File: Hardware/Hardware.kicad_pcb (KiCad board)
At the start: 2 copper layers, 91.4 x 142.2 mm, 47 parts, among them J1 Conn_01x04_Pin, J2 RJ45_LED_Shielded, J3 USB_A, SW1 SW_SPST, SW2 SW_Push, SW3 SW_Push, SW4 SW_Push, SW5 SW_Push, SW6 SW_Push, SW7 SW_Push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

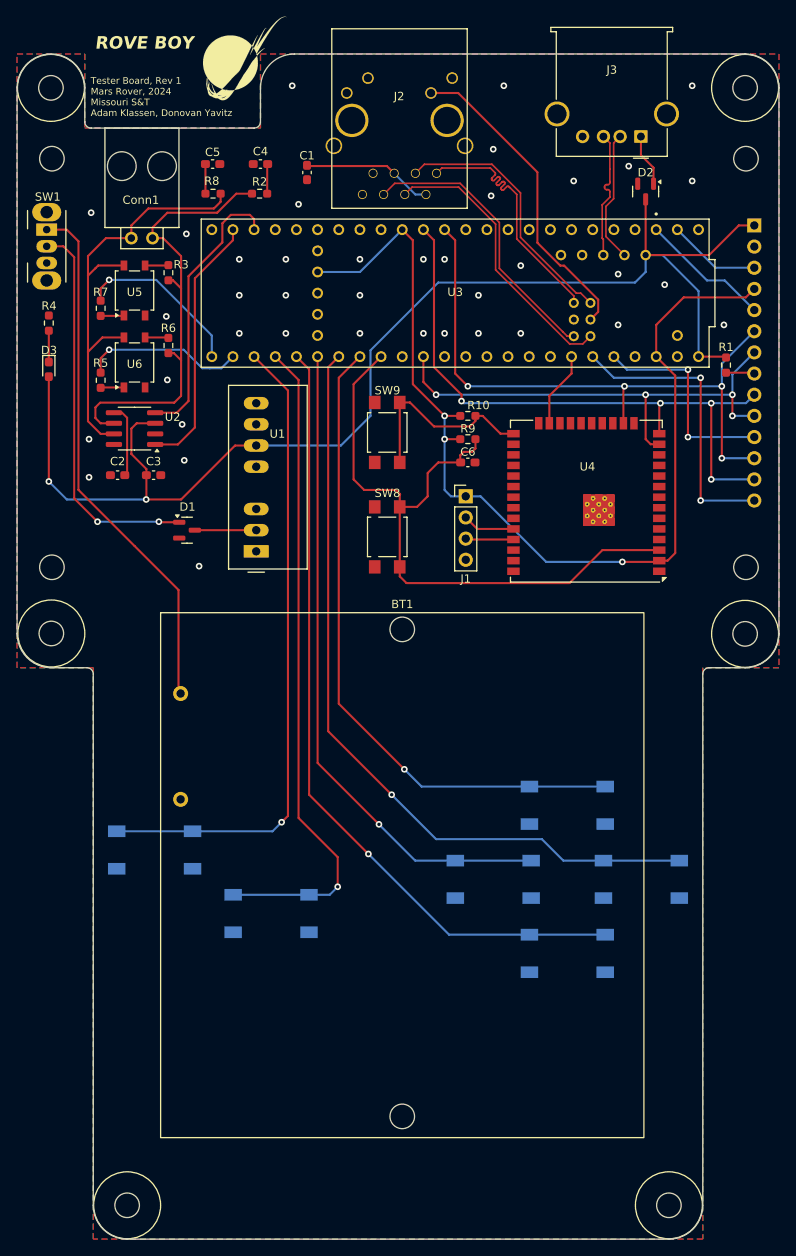
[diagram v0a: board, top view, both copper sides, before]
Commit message: fixed silkscreens and added servo tester
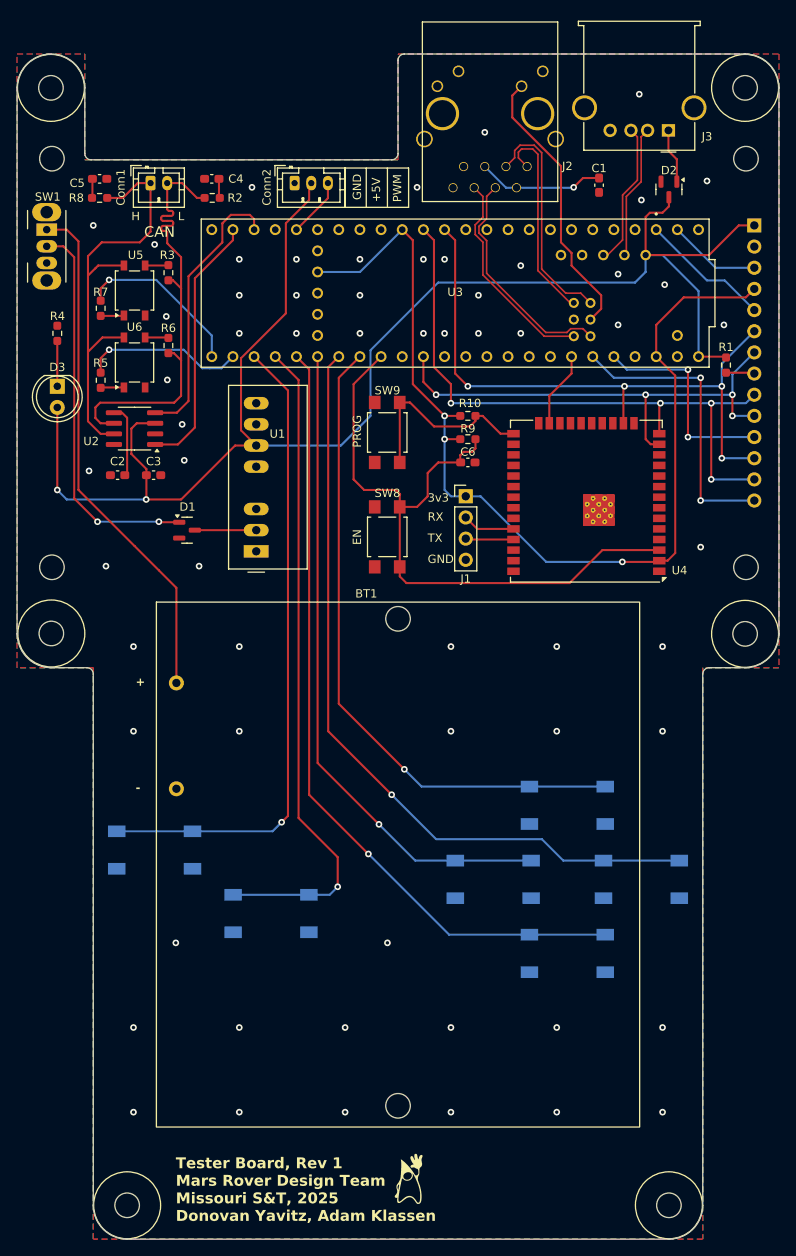
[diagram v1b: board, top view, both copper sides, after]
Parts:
- removed the G*** at (181.0, 61.5)
- added Conn2: Molex_SL_03, Connector_JST:JST_PH_B3B-PH-K_1x03_P2.00mm_Vertical, F.Cu at (187.0, 76.5)
- added G***: LOGO, Tester:duke, F.Cu at (200.7, 196.1)
- Conn1: footprint MRDT_Connectors:MOLEX_SL_02_Horizontal -> Connector_JST:JST_PH_B2B-PH-K_1x02_P2.00mm_Vertical
- D3: footprint LED_SMD:LED_0603_1608Metric_Pad1.05x0.95mm_HandSolder -> LED_THT:LED_D5.0mm
- moved C1 35.1 mm to (223.5, 76.7)
- moved C5 13.7 mm to (163.6, 75.9)
- moved R8 13.6 mm to (163.6, 78.2)
- moved J2 10.9 mm to (210.3, 55.1)
- moved Conn1 6.99 mm to (169.7, 76.5)
- moved C4 6.11 mm to (177.0, 75.9)
- moved R2 5.71 mm to (177.1, 78.2)
- moved J3 3.38 mm to (231.8, 70.1)
- moved D2 2.81 mm to (231.9, 77.2)
- moved D3 2.27 mm to (158.5, 100.8)
- moved R4 1.60 mm to (158.5, 94.5)
- moved BT1 1.37 mm to (199.4, 126.7)
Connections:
- U3 pad 28: unconnected-(U3-RX7-Pad28) -> PWM
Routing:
- net +5V: track 156.3 -> 190.4 mm
- net Rx-: track 34.2 -> 25.6 mm
- net PWM: track 0.00 -> 7.15 mm
- net Rx+: track 34.1 -> 27.4 mm
- net Tx+: track 31.4 -> 24.8 mm
- net LED: track 38.1 -> 33.4 mm
- net Tx-: track 31.5 -> 27.7 mm
- net Net-(D3-K): track 3.76 -> 5.44 mm
- net Net-(BT1-+): track 63.7 -> 62.3 mm
- net USB_D+: track 15.8 -> 17.3 mm
- net Net-(C4-Pad1): track 3.58 -> 2.33 mm
- net Net-(C5-Pad1): track 3.56 -> 2.31 mm
- net MISO: track 76.4 -> 77.3 mm
- net Net-(C1-Pad1): track 15.7 -> 15.3 mm, vias 0 -> 1
- net GND: vias 39 -> 61
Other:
- outline, holes or cut-outs redrawn
- board text added: "+"
- board text added: "+5V"
- board text added: "-"
- board text added: "3v3"
- board text added: "Accept"
- board text added: "CAN"
- board text added: "EN"
- board text added: "GND"
- board text added: "H"
- board text added: "L"
- board text added: "PROG"
- board text added: "PWM"
- board text added: "RX"
- board text added: "RoveMO"
- board text added: "SL_2_Panel_Mount"
- board text added: "SL_3_Panel_Mount"
- board text added: "TX"
- board text added: "Tester Board, Rev 1 Mars Rover Design Team Missouri S&T, 2025 Donovan Yavitz, Adam Klassen"
- board text removed: "Enter"
- board text removed: "ROVE BOY"
- board text removed: "Tester Board, Rev 1 Mars Rover, 2024 Missouri S&T Adam Klassen, Donovan Yavitz"

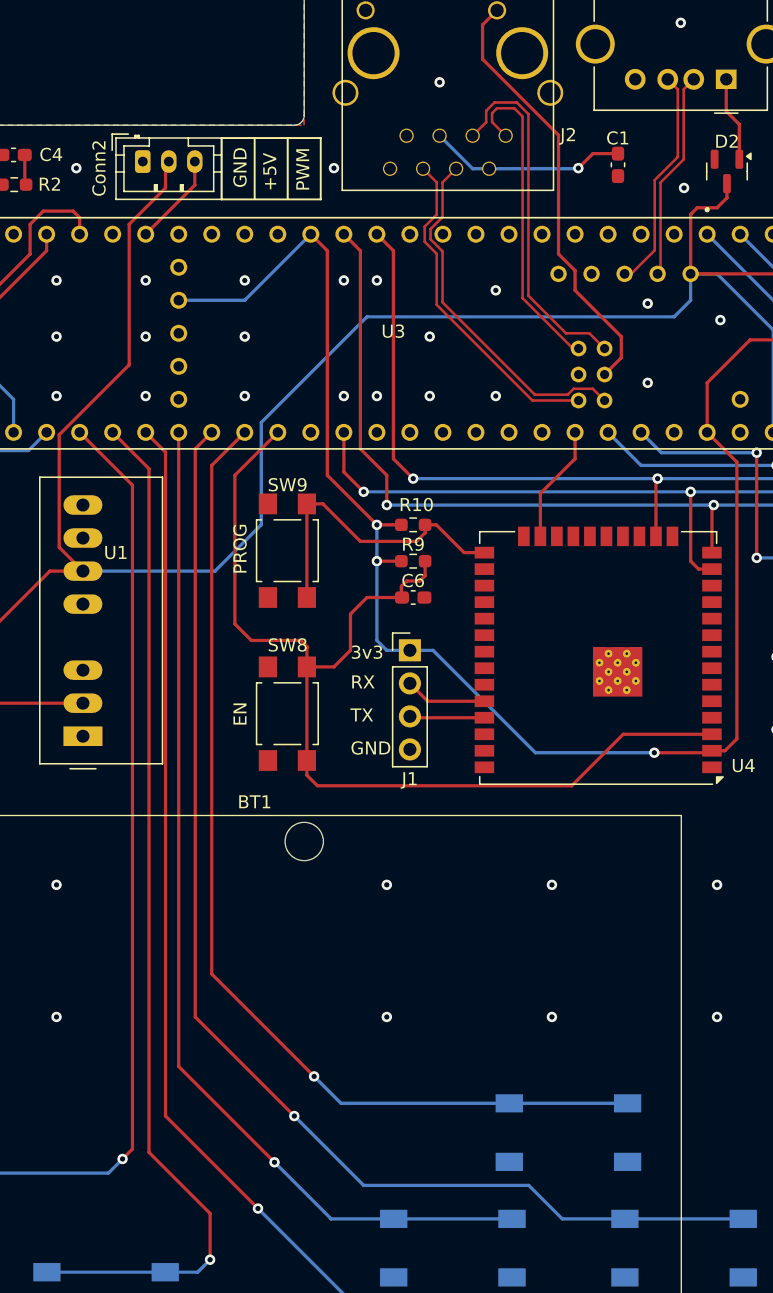
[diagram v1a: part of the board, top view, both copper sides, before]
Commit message: fixed skew on ethernet traces
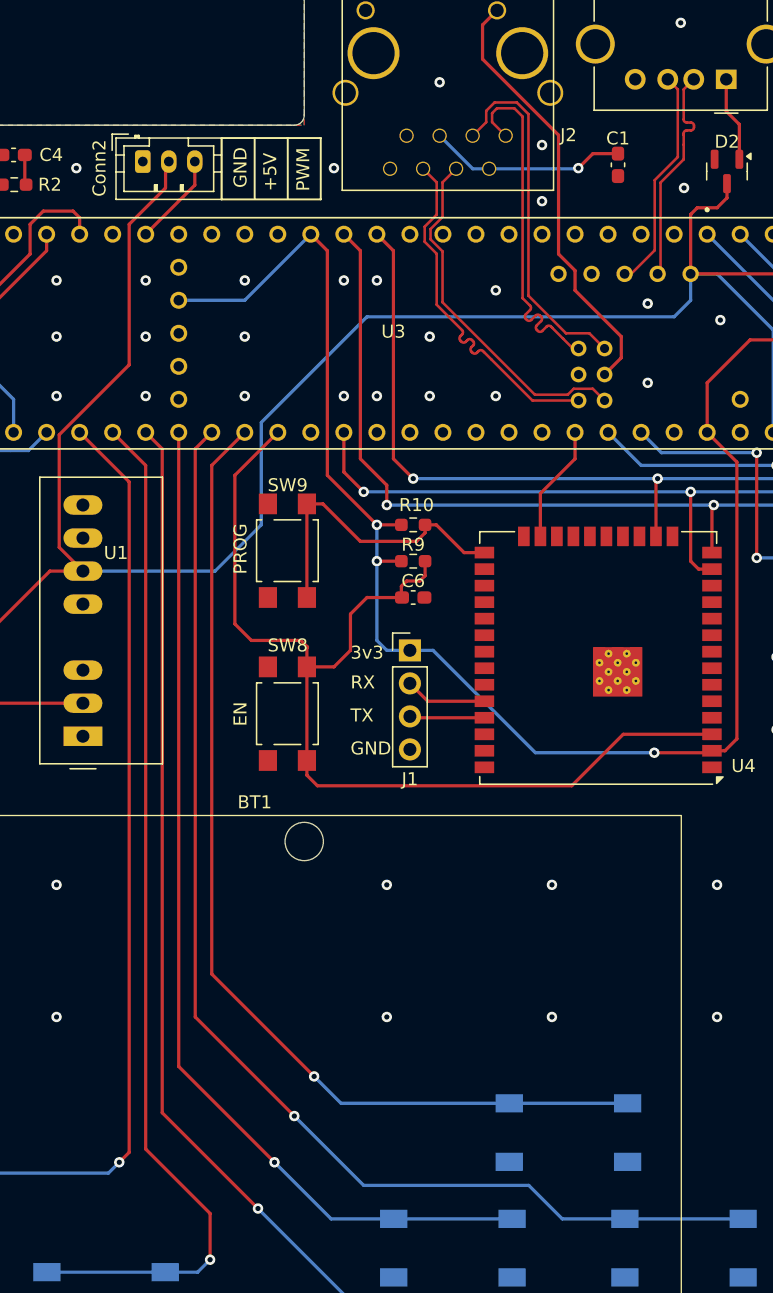
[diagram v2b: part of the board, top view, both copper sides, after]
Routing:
- net Tx+: track 24.8 -> 27.7 mm
- net Rx-: track 25.6 -> 27.4 mm
- net USB_D-: track 16.1 -> 17.3 mm
- net GND: vias 61 -> 63
